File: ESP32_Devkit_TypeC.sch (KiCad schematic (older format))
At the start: 49 parts, among them J1 USB_C_Receptacle_USB2.0, J2 Conn_01x19, J3 Conn_01x19, Q1 SS8050, Q2 SS8050, SW1 EN, SW2 BOOT, U1 MP2359, U2 CH340G, U3 ESP32-PICO-D4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

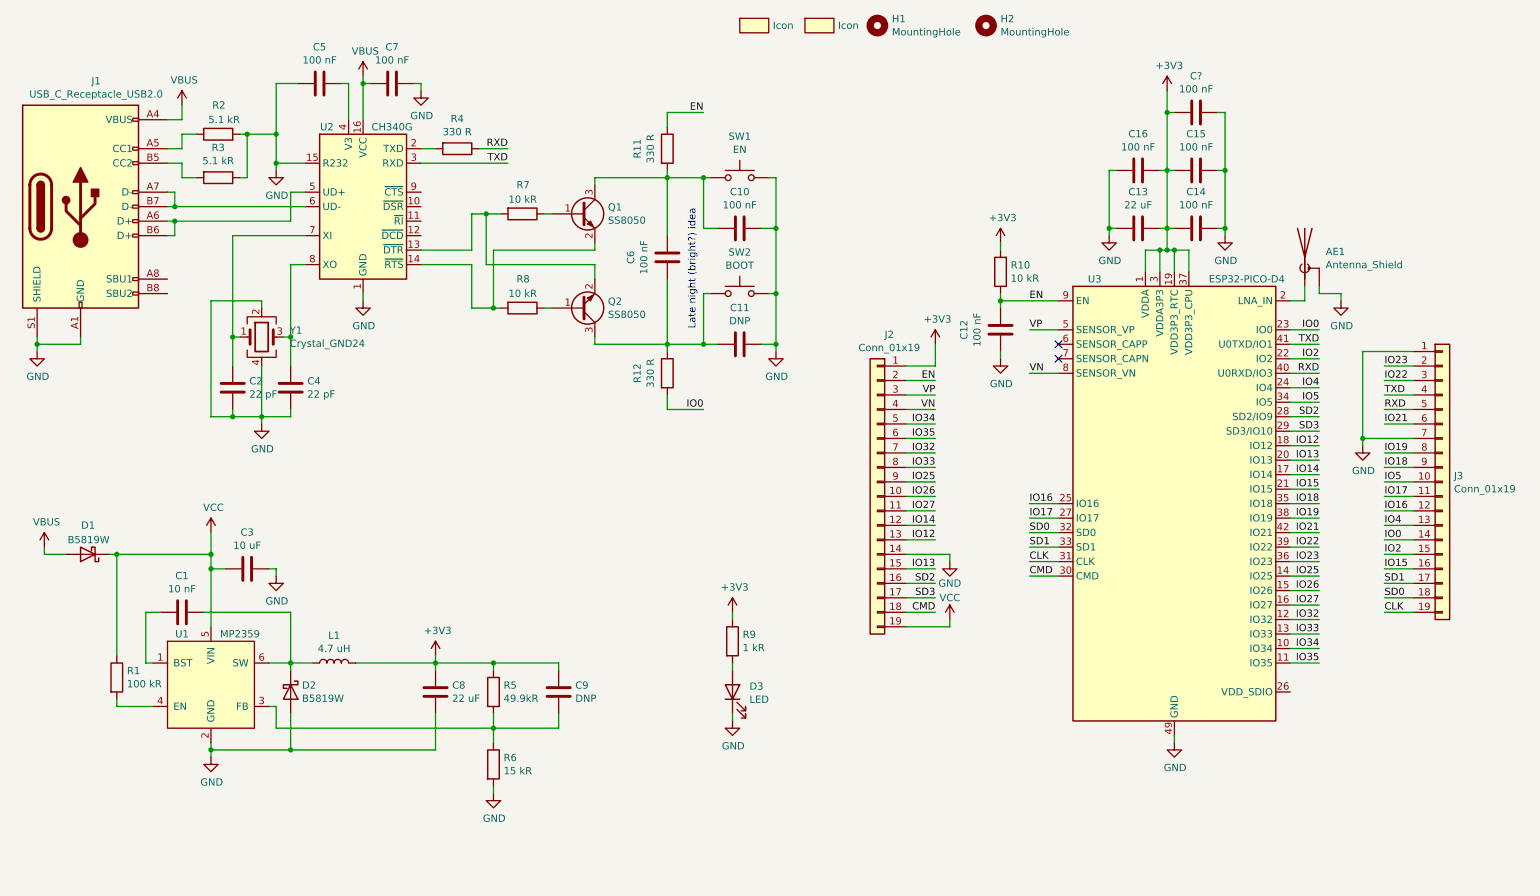
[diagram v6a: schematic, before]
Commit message: Rev D
Most importantly this revision improves reset/bootloader behaviour
by increasing the RC time constant of the reset RC network considerably.
(~50ms vs 1ms). This makes programming more reliable on machines with
high DTR/RTS setting delays or when working with USB over IP solutions.

Full list of changes:
* Improve reset/flash behaviour
* Eliminate 10k resistors
* Reduce brightness of power led
* Remove Corona warning
* Remove groundplane below antenna
* Eliminate cap from EN to IO0, causes boot issues
* Add input diode shorting jumper
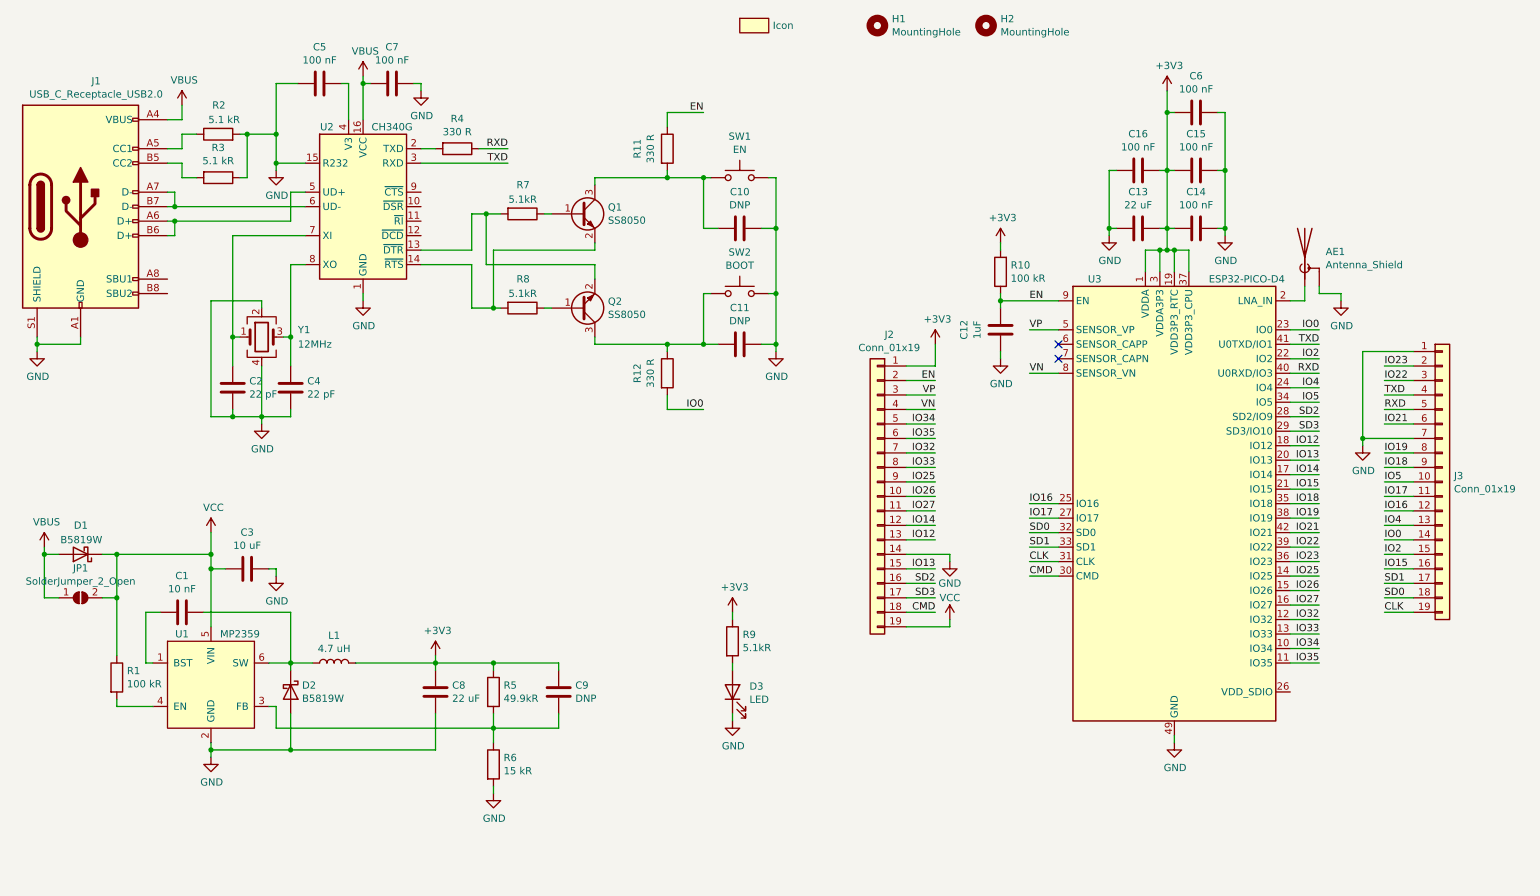
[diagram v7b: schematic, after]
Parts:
- removed C6: 100 nF, Capacitor_SMD:C_0402_1005Metric, symbol Device:C
- removed I1: Icon, Signs:Danger_RF_Corona, symbol Icon:Icon
- added JP1: SolderJumper_2_Open, Jumper:SolderJumper-2_P1.3mm_Open_Pad1.0x1.5mm, symbol Jumper:SolderJumper_2_Open
- C10: value 100 nF -> DNP; LCSC C1525 -> (none)
- C12: value 100 nF -> 1uF; LCSC C1525 -> C52923
- R10: value 10 kR -> 100 kR; LCSC C25744 -> C25741
- R7, R8: value 10 kR -> 5.1kR; LCSC C25744 -> C25905
- R9: value 1 kR -> 5.1kR; LCSC C11702 -> C25905
- Y1: value Crystal_GND24 -> 12MHz
- gave numbers to parts that had none: 1
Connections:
- net VBUS: now also JP1.1 (A)
- net VCC: now also JP1.2 (B)
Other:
- note removed: "Late night (bright?) idea"
- moved on the sheet: D1
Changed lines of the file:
@@
 encoding utf-8
 Sheet 1 1
-Title ""
-Date ""
-Rev ""
+Title "ESP32 DevKit Type C"
+Date "2020-09-29"
+Rev "D"
 Comp ""
 Comment1 ""
@@
 U 1 1 5EB3DDA3
 P 2550 2750
-F 0 "Y1" H 2744 2796 50  0000 L CNN
-F 1 "Crystal_GND24" H 2744 2705 50  0000 L CNN
+F 0 "Y1" H 2800 2800 50  0000 L CNN
+F 1 "12MHz" H 2800 2700 50  0000 L CNN
 F 2 "Crystal:Crystal_SMD_3225-4Pin_3.2x2.5mm" H 2550 2750 50  0001 C CNN
 F 3 "~" H 2550 2750 50  0001 C CNN
@@
 L Device:D_Schottky D1
 U 1 1 5EB66FE4
-P 1350 4250
-F 0 "D1" H 1300 4050 50  0000 L CNN
-F 1 "B5819W" H 1200 4150 50  0000 L CNN
-F 2 "Diode_SMD:D_SOD-123" H 1350 4250 50  0001 C CNN
-F 3 "~" H 1350 4250 50  0001 C CNN
-F 4 "C8598" V 1350 4250 50  0001 C CNN "LCSC"
-	1    1350 4250
+P 1300 4250
+F 0 "D1" H 1250 4050 50  0000 L CNN
+F 1 "B5819W" H 1150 4150 50  0000 L CNN
+F 2 "Diode_SMD:D_SOD-123" H 1300 4250 50  0001 C CNN
+F 3 "~" H 1300 4250 50  0001 C CNN
+F 4 "C8598" V 1300 4250 50  0001 C CNN "LCSC"
+	1    1300 4250
 	-1   0    0    1
 $EndComp
@@
 	1    0    0    -1
 $EndComp
-Wire Wire Line
-	1050 4200 1050 4250
-Wire Wire Line
-	1050 4250 1200 4250
 Wire Wire Line
 	2600 5000 2750 5000
@@
 	2750 4650 2750 5000
 Wire Wire Line
-	1550 4950 1550 4250
+	1550 4950 1550 4550
 Connection ~ 2200 4250
 Wire Wire Line
@@
 Connection ~ 1550 4250
 Wire Wire Line
-	1500 4250 1550 4250
-Wire Wire Line
 	2200 4100 2200 4250
 $Comp
@@
 P 5850 2000
 F 0 "C10" V 5598 2000 50  0000 C CNN
-F 1 "100 nF" V 5689 2000 50  0000 C CNN
+F 1 "DNP" V 5689 2000 50  0000 C CNN
 F 2 "Capacitor_SMD:C_0402_1005Metric" H 5888 1850 50  0001 C CNN
 F 3 "~" H 5850 2000 50  0001 C CNN
-F 4 "C1525" H 5850 2000 50  0001 C CNN "LCSC"
 	1    5850 2000
 	0    1    1    0
@@
 P 7650 2700
 F 0 "C12" V 7398 2700 50  0000 C CNN
-F 1 "100 nF" V 7489 2700 50  0000 C CNN
+F 1 "1uF" V 7489 2700 50  0000 C CNN
 F 2 "Capacitor_SMD:C_0402_1005Metric" H 7688 2550 50  0001 C CNN
 F 3 "~" H 7650 2700 50  0001 C CNN
-F 4 "C1525" H 7650 2700 50  0001 C CNN "LCSC"
+F 4 "C52923" H 7650 2700 50  0001 C CNN "LCSC"
 	1    7650 2700
 	1    0    0    -1
@@
 P 7650 2300
 F 0 "R10" H 7580 2254 50  0000 R CNN
-F 1 "10 kR" H 7580 2345 50  0000 R CNN
+F 1 "100 kR" H 7580 2345 50  0000 R CNN
 F 2 "Resistor_SMD:R_0402_1005Metric" V 7580 2300 50  0001 C CNN
 F 3 "~" H 7650 2300 50  0001 C CNN
-F 4 "C25744" H 7650 2300 50  0001 C CNN "LCSC"
+F 4 "C25741" H 7650 2300 50  0001 C CNN "LCSC"
 	1    7650 2300
 	-1   0    0    1
@@
 	4850 1700 4850 1650
 $Comp
-L Device:R R7
-U 1 1 5F039C72
-P 4350 1900
-F 0 "R7" V 4150 1950 50  0000 R CNN
-F 1 "10 kR" V 4250 2000 50  0000 R CNN
-F 2 "Resistor_SMD:R_0402_1005Metric" V 4280 1900 50  0001 C CNN
-F 3 "~" H 4350 1900 50  0001 C CNN
-F 4 "C25744" H 4350 1900 50  0001 C CNN "LCSC"
-	1    4350 1900
-	0    1    1    0
-$EndComp
-$Comp
 L Device:R R8
 U 1 1 5F045B80
 P 4350 2550
 F 0 "R8" V 4150 2600 50  0000 R CNN
-F 1 "10 kR" V 4250 2650 50  0000 R CNN
+F 1 "5.1kR" V 4250 2650 50  0000 R CNN
 F 2 "Resistor_SMD:R_0402_1005Metric" V 4280 2550 50  0001 C CNN
 F 3 "~" H 4350 2550 50  0001 C CNN
-F 4 "C25744" H 4350 2550 50  0001 C CNN "LCSC"
+F 4 " C25905" H 4350 2550 50  0001 C CNN "LCSC"
 	1    4350 2550
 	0    1    1    0
@@
 P 5800 4850
 F 0 "R9" H 5870 4896 50  0000 L CNN
-F 1 "1 kR" H 5870 4805 50  0000 L CNN
+F 1 "5.1kR" H 5870 4805 50  0000 L CNN
 F 2 "Resistor_SMD:R_0402_1005Metric" V 5730 4850 50  0001 C CNN
 F 3 "~" H 5800 4850 50  0001 C CNN
-F 4 "C11702" H 5800 4850 50  0001 C CNN "LCSC"
+F 4 " C25905" H 5800 4850 50  0001 C CNN "LCSC"
 	1    5800 4850
 	1    0    0    -1
@@
 	3200 5000 3750 5000
 $Comp
-L Icon:Icon I1
-U 1 1 5F3C704C
-P 6400 600
-F 0 "I1" H 6400 600 50  0001 C CNN
-F 1 "Icon" H 6528 600 50  0000 L CNN
-F 2 "Signs:Danger_RF_Corona" H 6400 600 50  0001 C CNN
-F 3 "" H 6400 600 50  0001 C CNN
-	1    6400 600
-	1    0    0    -1
-$EndComp
-$Comp
 L Mechanical:MountingHole H1
 U 1 1 5F3DD188
@@
 Connection ~ 5600 1650
 Connection ~ 5600 2800
-$Comp
-L Device:C C6
-U 1 1 5ECF6C76
-P 5350 2200
-F 0 "C6" V 5098 2200 50  0000 C CNN
-F 1 "100 nF" V 5189 2200 50  0000 C CNN
-F 2 "Capacitor_SMD:C_0402_1005Metric" H 5388 2050 50  0001 C CNN
-F 3 "~" H 5350 2200 50  0001 C CNN
-F 4 "C1525" H 5350 2200 50  0001 C CNN "LCSC"
-	1    5350 2200
-	1    0    0    -1
-$EndComp
-Wire Wire Line
-	5350 2050 5350 1650
 Connection ~ 5350 1650
 Wire Wire Line
@@
 Wire Wire Line
 	4850 2800 5350 2800
-Wire Wire Line
-	5350 2350 5350 2800
 Connection ~ 5350 2800
 Wire Wire Line
 	5350 2800 5600 2800
-Text Notes 5550 2700 1    50   ~ 0
-Late night (bright?) idea
 $Comp
 L Device:R R11
@@
 Connection ~ 8400 2000
 $Comp
-L Device:C C?
+L Device:C C6
 U 1 1 5EDFD5B9
 P 9000 1200
-F 0 "C?" V 8748 1200 50  0000 C CNN
+F 0 "C6" V 8748 1200 50  0000 C CNN
 F 1 "100 nF" V 8839 1200 50  0000 C CNN
 F 2 "Capacitor_SMD:C_0402_1005Metric" H 9038 1050 50  0001 C CNN
@@
 	8800 1200 8800 1050
 Connection ~ 8800 1200
+$Comp
+L Device:R R7
+U 1 1 5F039C72
+P 4350 1900
+F 0 "R7" V 4150 1950 50  0000 R CNN
+F 1 "5.1kR" V 4250 2000 50  0000 R CNN
+F 2 "Resistor_SMD:R_0402_1005Metric" V 4280 1900 50  0001 C CNN
+F 3 "~" H 4350 1900 50  0001 C CNN
+F 4 " C25905" H 4350 1900 50  0001 C CNN "LCSC"
+	1    4350 1900
+	0    1    1    0
+$EndComp
+$Comp
+L Jumper:SolderJumper_2_Open JP1
+U 1 1 5F7702D8
+P 1300 4550
+F 0 "JP1" H 1300 4755 50  0000 C CNN
+F 1 "SolderJumper_2_Open" H 1300 4664 50  0000 C CNN
+F 2 "Jumper:SolderJumper-2_P1.3mm_Open_Pad1.0x1.5mm" H 1300 4550 50  0001 C CNN
+F 3 "~" H 1300 4550 50  0001 C CNN
+	1    1300 4550
+	1    0    0    -1
+$EndComp
+Connection ~ 1550 4550
+Wire Wire Line
+	1550 4550 1550 4250
+Wire Wire Line
+	1050 4200 1050 4250
+Wire Wire Line
+	1450 4250 1550 4250
+Wire Wire Line
+	1450 4550 1550 4550
+Wire Wire Line
+	1150 4250 1050 4250
+Connection ~ 1050 4250
+Wire Wire Line
+	1050 4250 1050 4550
+Wire Wire Line
+	1050 4550 1150 4550
 $EndSCHEMATC

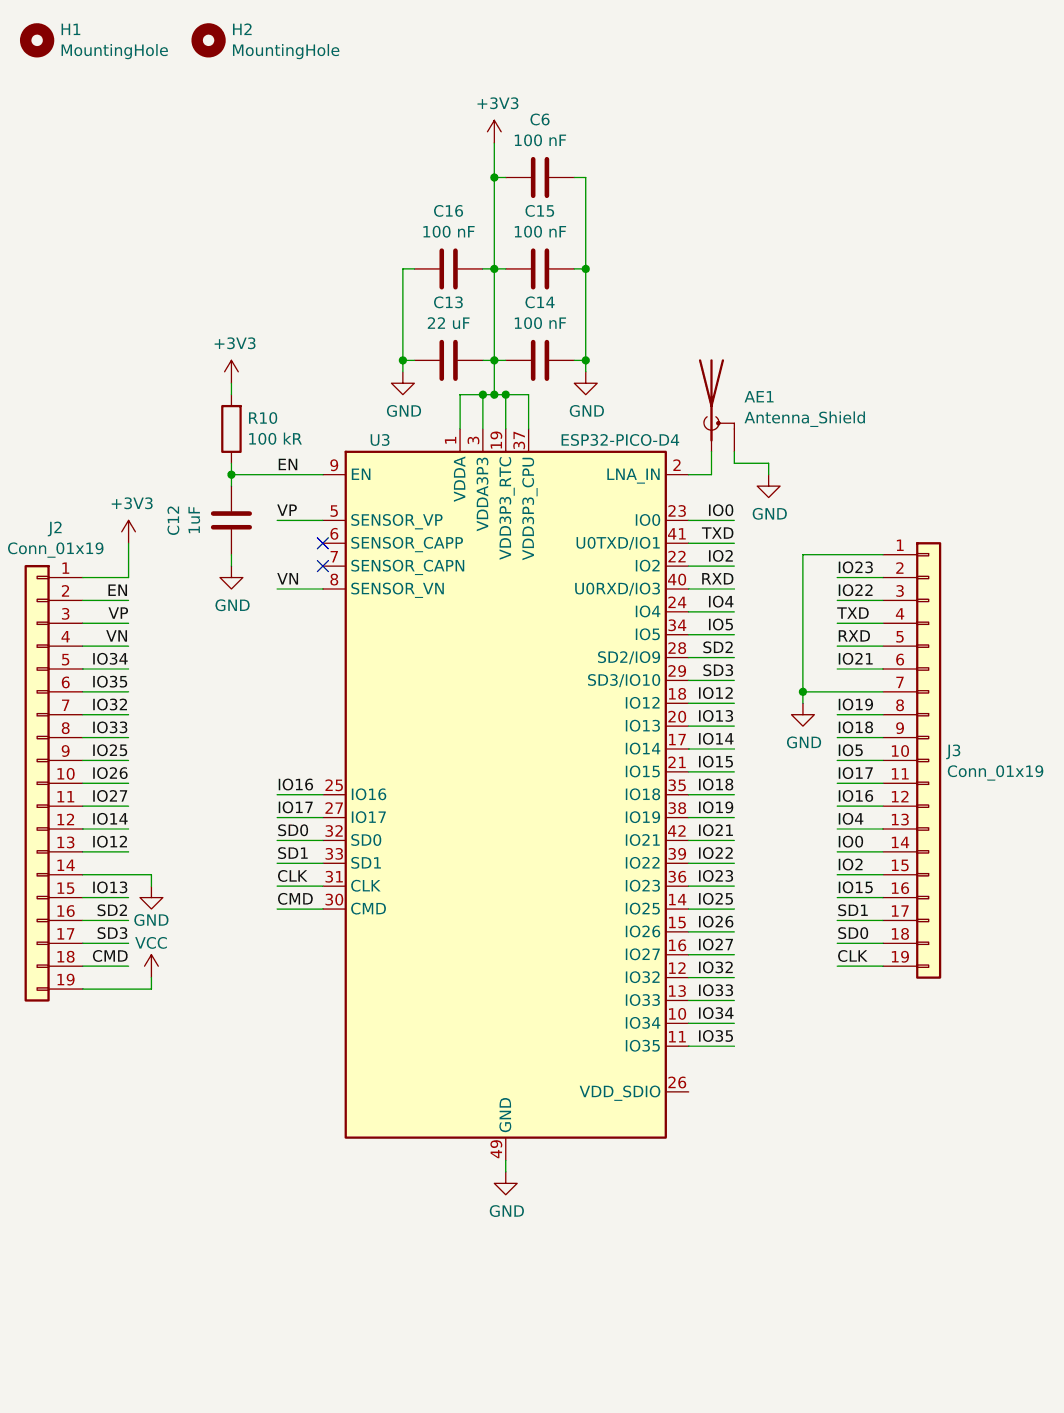
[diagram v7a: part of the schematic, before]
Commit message: Rev E better bypassing
This revision improves upon the bypassing of the ESP32 Pico D4.
The previous bypassing was not satisfactory to me and I fear it
might cause issues under high load conditions.
Bypassing is improved by adding an additional 10uF capacitor to
each power pin.
Additionally a third 22uF capacitor has been added to icrease bulk
capacitance
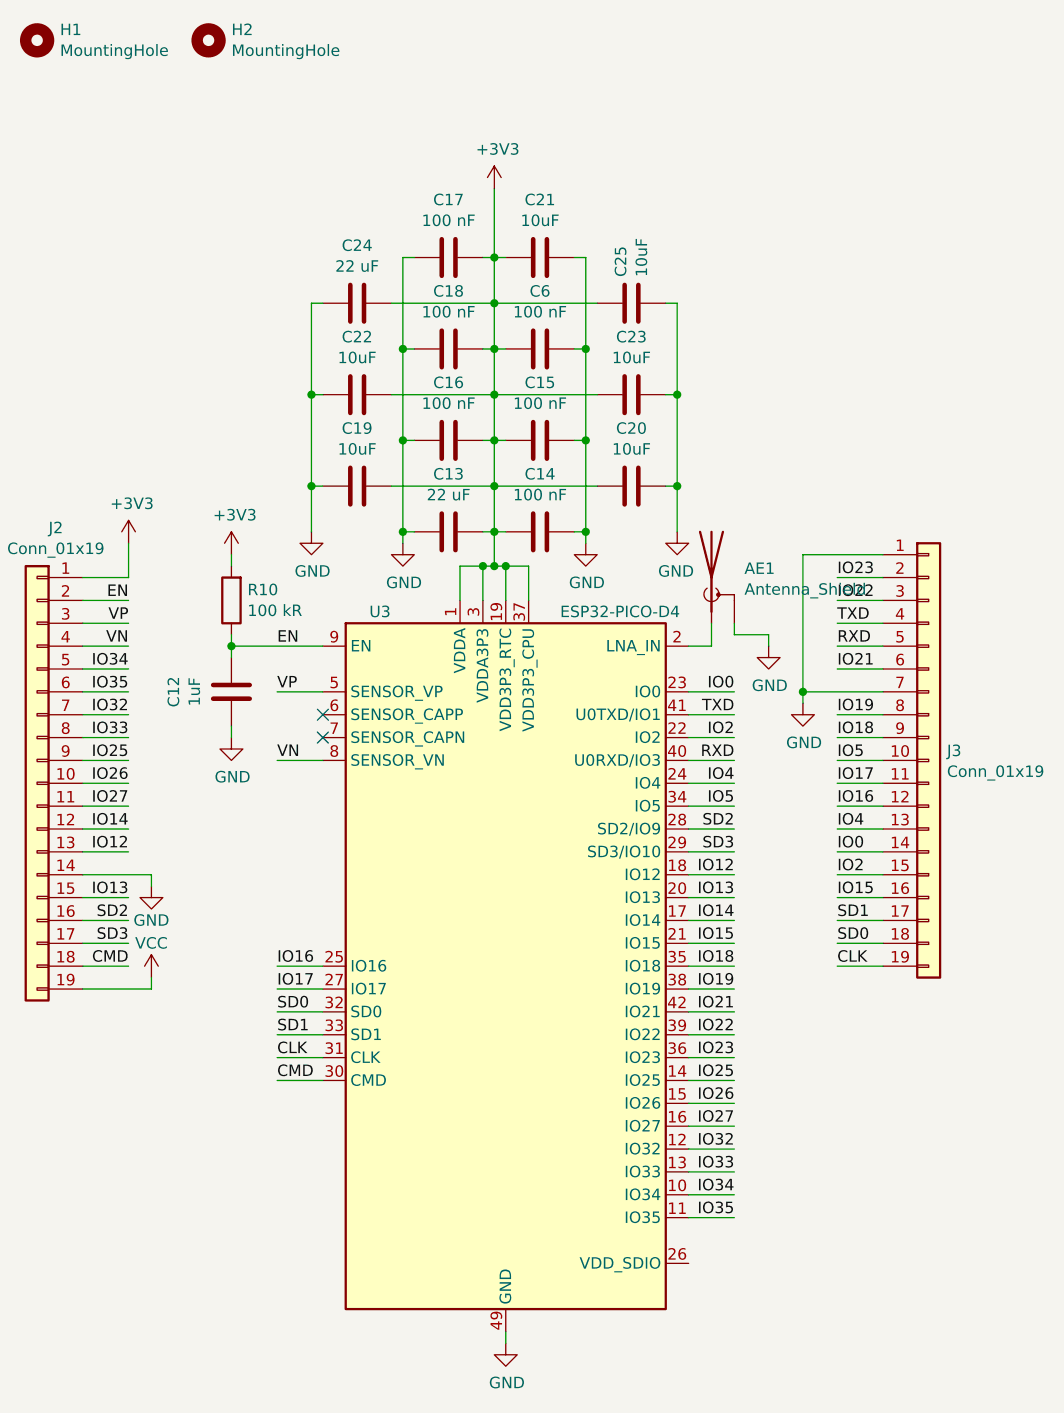
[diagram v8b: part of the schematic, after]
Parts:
- added C17, C18: 100 nF, Capacitor_SMD:C_0402_1005Metric, symbol Device:C
- added C19, C20, C21, C22: 10uF, Capacitor_SMD:C_0402_1005Metric, symbol Device:C
- added C23, C25: 10uF, Capacitor_SMD:C_0603_1608Metric, symbol Device:C
- added C24: 22 uF, Capacitor_SMD:C_0603_1608Metric, symbol Device:C
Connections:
- net +3V3: now also C17.1, C18.1, C19.1, C20.2, C21.2, C22.1, C23.2, C24.1, C25.1
- net GND: now also C17.2, C18.2, C19.2, C20.1, C21.1, C22.2, C23.1, C24.2, C25.2
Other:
- moved on the sheet: AE1, C12, C13, C14, C15, C16, C6, R10, U3
